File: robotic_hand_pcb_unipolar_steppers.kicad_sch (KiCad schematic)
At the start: 15 parts, among them J5 JST 1x5 Male, J6 JST 1x5 Male, J7 JST 1x5 Male, J8 JST 1x5 Male, J9 JST 1x5 Male, U5 ULN2003ADR, U6 ULN2003ADR, U7 ULN2003ADR, U8 ULN2003ADR, U9 ULN2003ADR

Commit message: Add 5V buck regulator
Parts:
- renumbered C22 to C26, C23 to C27, C24 to C28, C25 to C29, C26 to C30, U9 to U10, U5 to U6, U6 to U7, U7 to U8, U8 to U9

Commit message: Update for WIP changes
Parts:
- renumbered C26 to C25, C27 to C26, C28 to C27, C29 to C28, C30 to C29, J7 to J10, J8 to J11, J9 to J12, J5 to J8, J6 to J9

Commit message: Add WIP schematic changes
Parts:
- renumbered C25 to C38, C26 to C39, C27 to C40, C28 to C41, C29 to C42, J8 to J18, J9 to J19, J10 to J20, J11 to J21, J12 to J22, U6 to U14, U7 to U15, U8 to U16, U9 to U17, U10 to U18
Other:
- note added: "Unipoloar Stepper Motor Drivers"
- moved on the sheet: C38, C39, C40, C41, C42, J18, J19, J20, J21, J22, U14, U15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

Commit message: Assign footprints
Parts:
- J18, J19, J20, J21, J22: footprint (none) -> Connector_PinHeader_2.54mm:PinHeader_1x05_P2.54mm_Vertical
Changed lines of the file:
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@@
 			)
 		)
-		(property "Footprint" ""
+		(property "Footprint" "Connector_PinHeader_2.54mm:PinHeader_1x05_P2.54mm_Vertical"
 			(at 146.05 92.71 0)
 			(effects
@@
 			)
 		)
-		(property "Footprint" ""
+		(property "Footprint" "Connector_PinHeader_2.54mm:PinHeader_1x05_P2.54mm_Vertical"
 			(at 69.85 41.91 0)
 			(effects
@@
 			)
 		)
-		(property "Footprint" ""
+		(property "Footprint" "Connector_PinHeader_2.54mm:PinHeader_1x05_P2.54mm_Vertical"
 			(at 69.85 143.51 0)
 			(effects
@@
 			)
 		)
-		(property "Footprint" ""
+		(property "Footprint" "Connector_PinHeader_2.54mm:PinHeader_1x05_P2.54mm_Vertical"
 			(at 69.85 92.71 0)
 			(effects
@@
 			)
 		)
-		(property "Footprint" ""
+		(property "Footprint" "Connector_PinHeader_2.54mm:PinHeader_1x05_P2.54mm_Vertical"
 			(at 146.05 41.91 0)
 			(effects

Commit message: Cleanup and remove unneeded connectors
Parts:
- renumbered J18 to J13, J19 to J14, J20 to J15, J21 to J16, J22 to J17
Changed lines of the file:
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@@
 		(on_board yes)
 		(dnp no)
-		(property "Reference" "J21"
+		(property "Reference" "J16"
 			(at 146.558 87.884 0)
 			(effects
@@
 			(project "robotic_hand_pcb"
 				(path "/96df9010-a1f8-4419-aac0-9388de87cb21/519c2916-f1e5-4bf2-b7d2-8398d436960c"
-					(reference "J21")
+					(reference "J16")
 					(unit 1)
 				)
@@
 		(on_board yes)
 		(dnp no)
-		(property "Reference" "J18"
+		(property "Reference" "J13"
 			(at 70.358 37.084 0)
 			(effects
@@
 			(project "robotic_hand_pcb"
 				(path "/96df9010-a1f8-4419-aac0-9388de87cb21/519c2916-f1e5-4bf2-b7d2-8398d436960c"
-					(reference "J18")
+					(reference "J13")
 					(unit 1)
 				)
@@
 		(on_board yes)
 		(dnp no)
-		(property "Reference" "J22"
+		(property "Reference" "J17"
 			(at 70.358 138.684 0)
 			(effects
@@
 			(project "robotic_hand_pcb"
 				(path "/96df9010-a1f8-4419-aac0-9388de87cb21/519c2916-f1e5-4bf2-b7d2-8398d436960c"
-					(reference "J22")
+					(reference "J17")
 					(unit 1)
 				)
@@
 		(on_board yes)
 		(dnp no)
-		(property "Reference" "J20"
+		(property "Reference" "J15"
 			(at 70.358 87.884 0)
 			(effects
@@
 			(project "robotic_hand_pcb"
 				(path "/96df9010-a1f8-4419-aac0-9388de87cb21/519c2916-f1e5-4bf2-b7d2-8398d436960c"
-					(reference "J20")
+					(reference "J15")
 					(unit 1)
 				)
@@
 		(on_board yes)
 		(dnp no)
-		(property "Reference" "J19"
+		(property "Reference" "J14"
 			(at 146.558 37.084 0)
 			(effects
@@
 			(project "robotic_hand_pcb"
 				(path "/96df9010-a1f8-4419-aac0-9388de87cb21/519c2916-f1e5-4bf2-b7d2-8398d436960c"
-					(reference "J19")
-					(unit 1)
-				)
+					(reference "J14")
+					(unit 1)
+				)

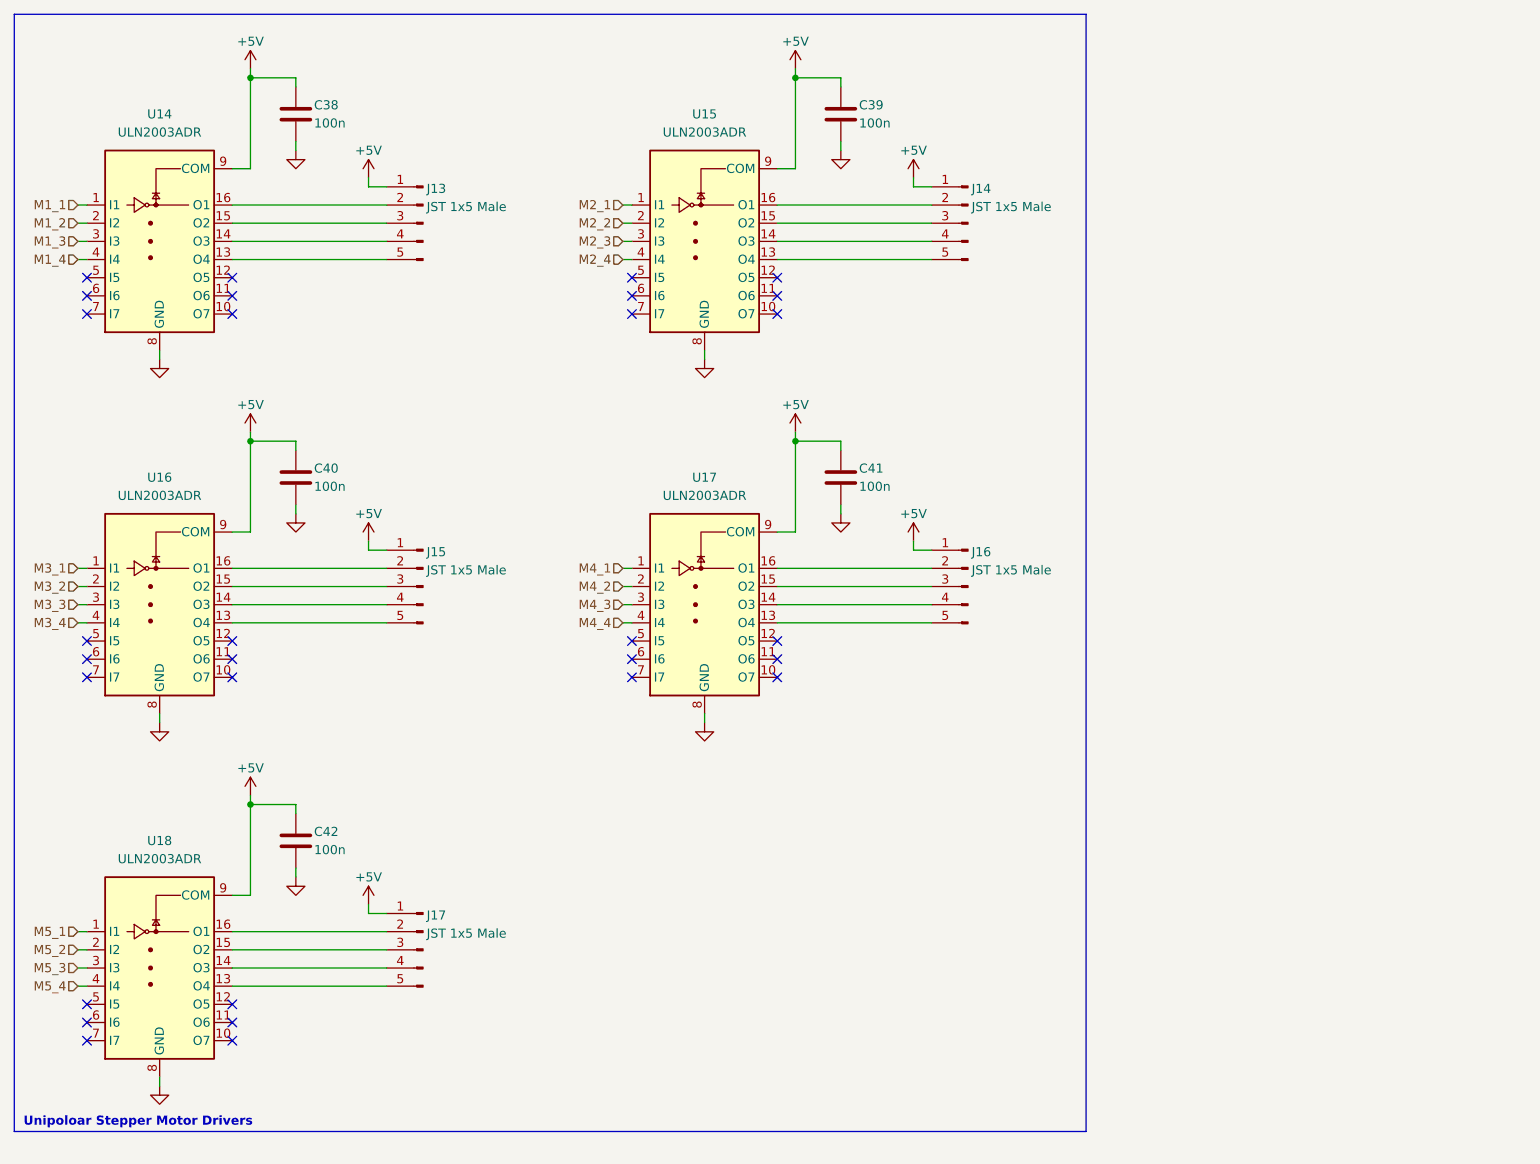
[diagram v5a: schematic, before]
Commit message: Add WIP PCB layout and routing
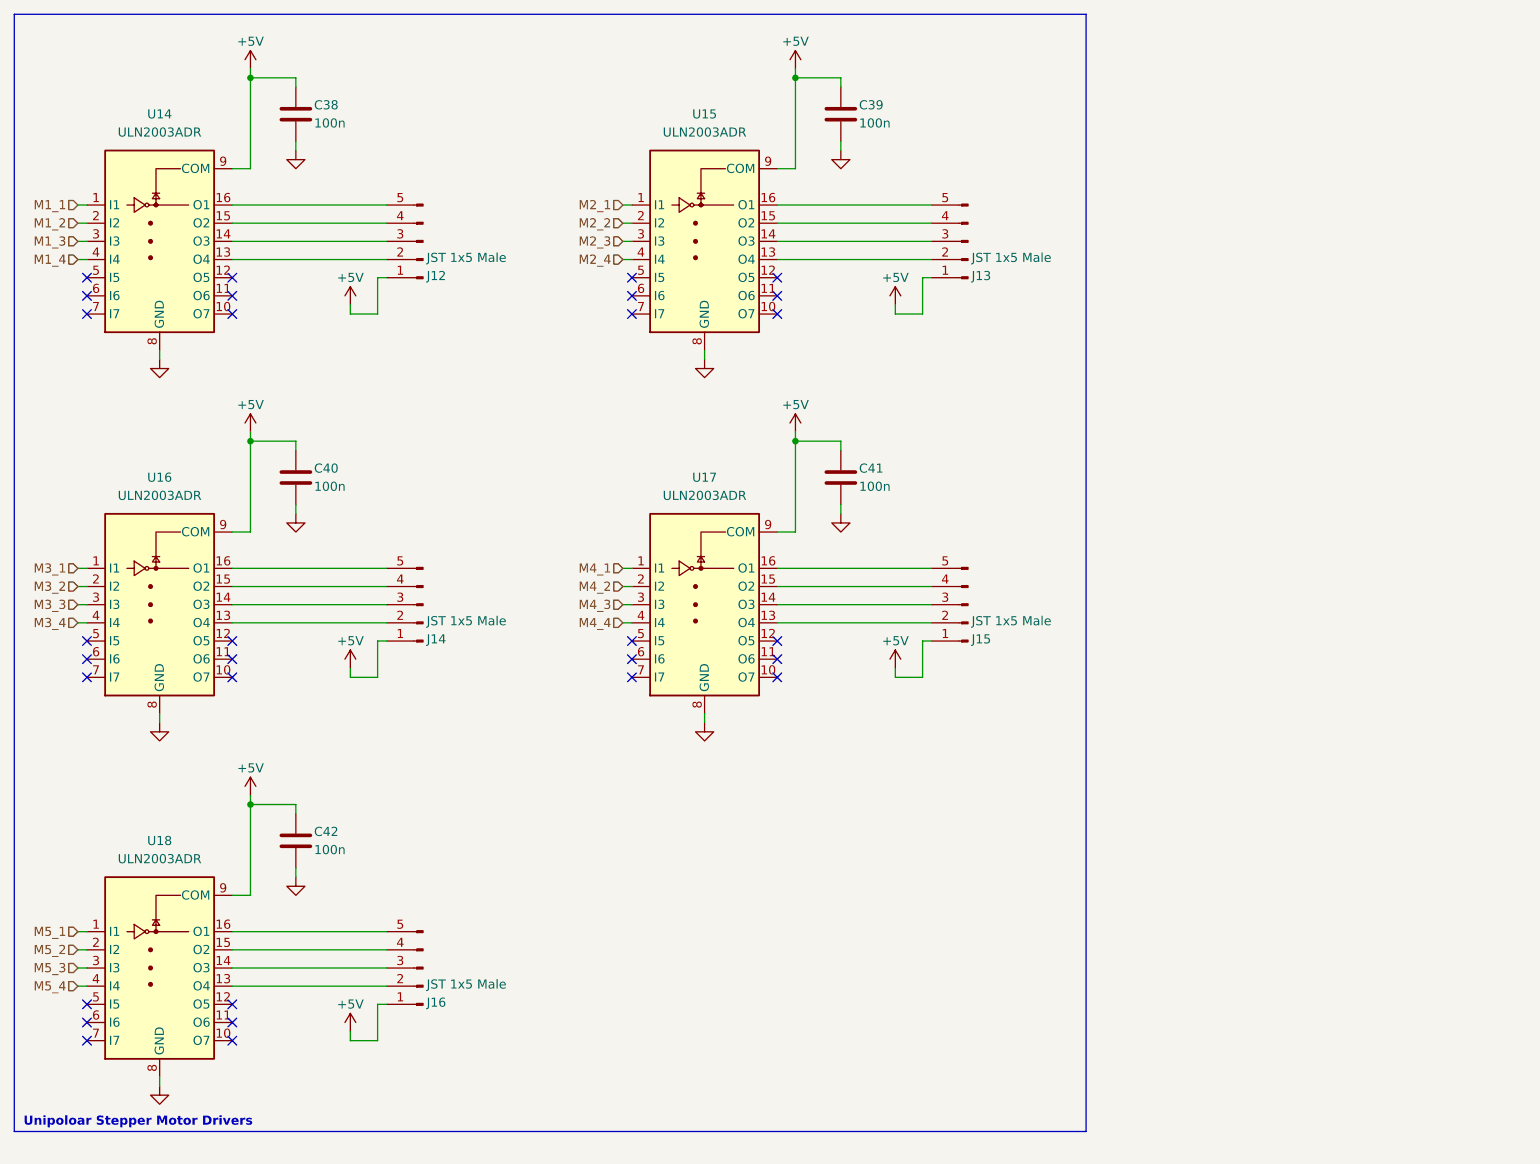
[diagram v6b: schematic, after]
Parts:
- removed J17: JST 1x5 Male, Connector_PinHeader_2.54mm:PinHeader_1x05_P2.54mm_Vertical, symbol Connector:Conn_01x05_Pin
- added J12: JST 1x5 Male, Connector_PinHeader_2.54mm:PinHeader_1x05_P2.54mm_Vertical, symbol Connector:Conn_01x05_Pin
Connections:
- net +5V: now also J12.1 (Pin_1)
- net at U17.16 (O1): now also J15.5 (Pin_5); no longer J16.2 (Pin_2)
- net at U17.15 (O2): now also J15.4 (Pin_4); no longer J16.3 (Pin_3)
- net at U17.14 (O3): now also J15.3 (Pin_3); no longer J16.4 (Pin_4)
- net at U17.13 (O4): now also J15.2 (Pin_2); no longer J16.5 (Pin_5)
- net at J13.2 (Pin_2): now also U15.13 (O4); no longer U14.16 (O1)
- net at J13.3 (Pin_3): now also U15.14 (O3); no longer U14.15 (O2)
- net at J13.4 (Pin_4): now also U15.15 (O2); no longer U14.14 (O3)
- net at J13.5 (Pin_5): now also U15.16 (O1); no longer U14.13 (O4)
- net at U18.13 (O4): now also J16.2 (Pin_2)
- net at U18.14 (O3): now also J16.3 (Pin_3)
- net at U18.15 (O2): now also J16.4 (Pin_4)
- net at U18.16 (O1): now also J16.5 (Pin_5)
- net at U16.13 (O4): now also J14.2 (Pin_2); no longer J15.5 (Pin_5)
- net at U16.14 (O3): now also J14.3 (Pin_3); no longer J15.4 (Pin_4)
- net at U16.15 (O2): now also J14.4 (Pin_4); no longer J15.3 (Pin_3)
- net at U16.16 (O1): now also J14.5 (Pin_5); no longer J15.2 (Pin_2)
- new net: J12.2 (Pin_2), U14.13 (O4)
- new net: J12.3 (Pin_3), U14.14 (O3)
- new net: J12.4 (Pin_4), U14.15 (O2)
- new net: J12.5 (Pin_5), U14.16 (O1)

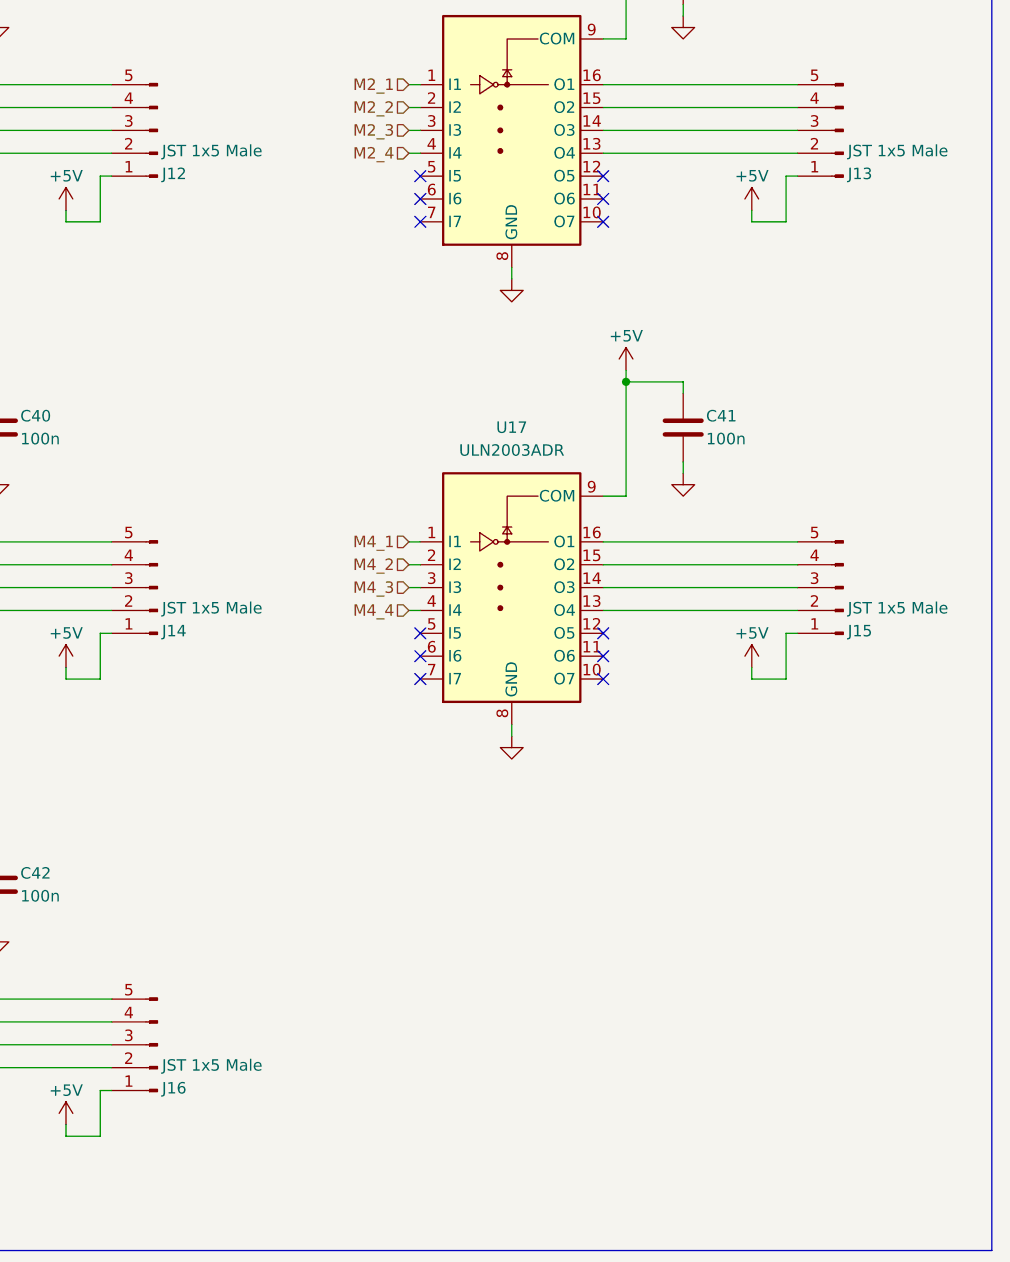
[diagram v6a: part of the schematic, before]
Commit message: Update WIP, clean up stepper drivers
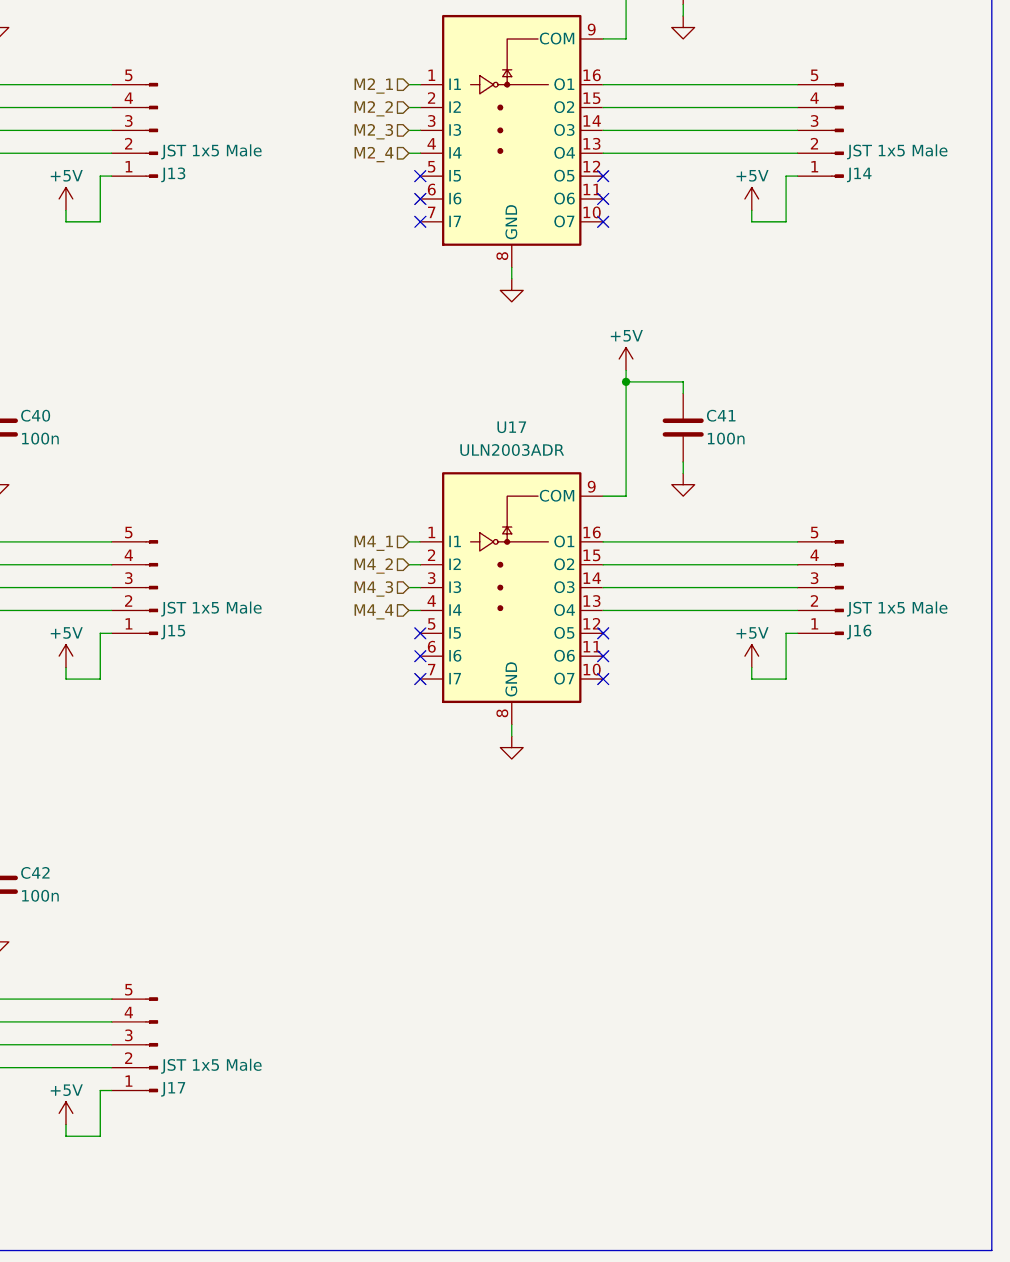
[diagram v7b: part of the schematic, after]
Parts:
- renumbered J12 to J13, J13 to J14, J14 to J15, J15 to J16, J16 to J17
